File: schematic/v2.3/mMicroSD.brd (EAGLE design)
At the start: 38 x 18 mm, 23 parts, among them IC1 MAX3392, IC2 ATMEGA328, IC3 AD8531, J1 ISPTOUCH, M1 NTJD5121N

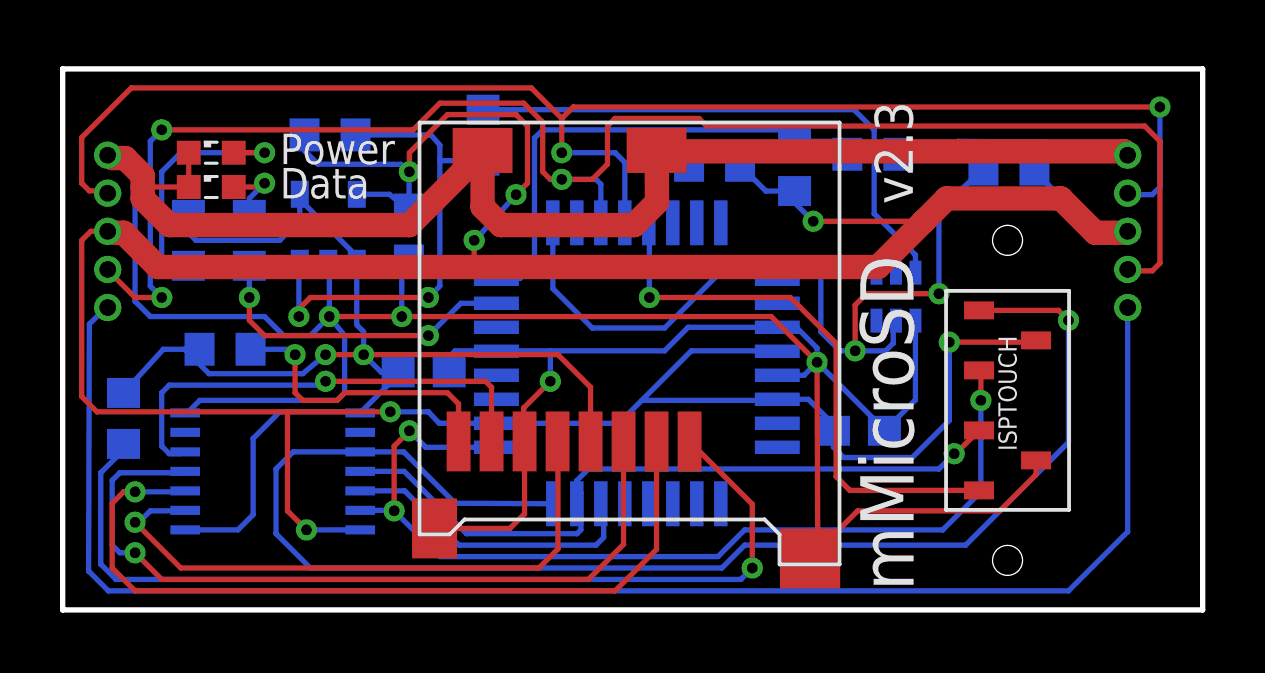
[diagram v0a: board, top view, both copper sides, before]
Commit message: Added some silkscreen to the board to make the orientation of two close resistors more apparent
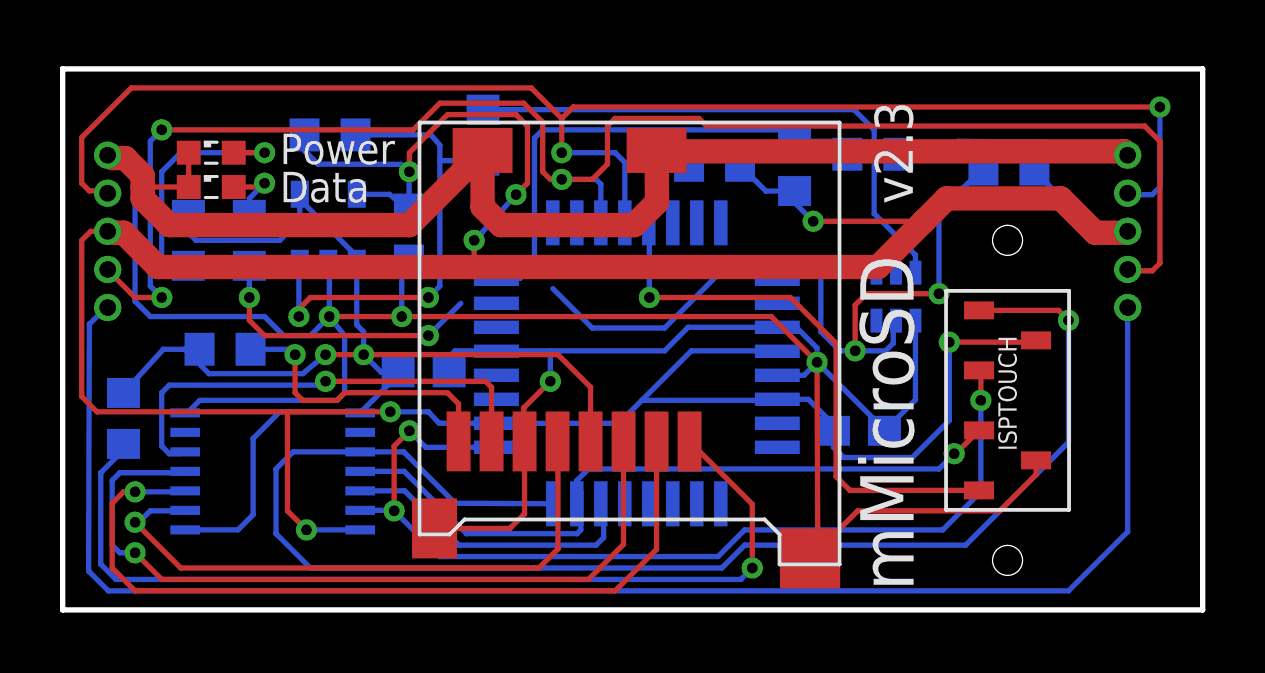
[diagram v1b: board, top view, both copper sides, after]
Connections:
- net N$10 renamed GATE
- net N$17 renamed ADC_LINE
- net N$3 renamed DATA_LED
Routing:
- net GATE: track 27.7 -> 25.5 mm
- net DATA_LED: track 10.7 -> 9.52 mm
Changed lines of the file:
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@@
 <?xml version="1.0" encoding="utf-8"?>
 <!DOCTYPE eagle SYSTEM "eagle.dtd">
-<eagle version="7.1.0">
+<eagle version="7.2.0">
 <drawing>
 <settings>
@@
 <text x="28.338990625" y="13.5300125" size="1.27" layer="21" font="vector" rot="R90">v2.3</text>
 <text x="7.239" y="14.859" size="1.016" layer="21" font="vector">Power</text>
-<text x="7.239" y="13.716" size="1.016" layer="21" font="vector">Data</text>
+<text x="7.239" y="13.589" size="1.016" layer="21" font="vector">Data</text>
+<wire x1="5.207" y1="11.176" x2="5.207" y2="13.335" width="0.4064" layer="22"/>
+<wire x1="6.985" y1="11.049" x2="6.985" y2="13.462" width="0.2032" layer="22"/>
+<wire x1="3.302" y1="13.462" x2="3.302" y2="11.049" width="0.2032" layer="22"/>
 </plain>
 <attributes>
@@
 <wire x1="4.203" y1="14.097" x2="2.667" y2="14.097" width="0.1778" layer="1"/>
 </signal>
-<signal name="N$10">
+<signal name="GATE">
 <contactref element="IC2" pad="25"/>
 <contactref element="M1" pad="2"/>
@@
 <wire x1="27.686" y1="8.89" x2="27.686" y2="9.552025" width="0.1778" layer="16"/>
 <wire x1="27.686" y1="9.552025" x2="27.7759125" y2="9.6419375" width="0.1778" layer="16"/>
-<wire x1="16.339925" y1="12.90348125" x2="16.339925" y2="10.711075" width="0.1778" layer="16"/>
 <wire x1="16.339925" y1="10.711075" x2="17.653" y2="9.398" width="0.1778" layer="16"/>
 <wire x1="17.653" y1="9.398" x2="20.066" y2="9.398" width="0.1778" layer="16"/>
@@
 <wire x1="29.21" y1="10.541" x2="29.21" y2="13.337909375" width="0.1778" layer="16"/>
 <wire x1="29.21" y1="13.337909375" x2="30.692103125" y2="14.6930125" width="0.1778" layer="16"/>
+<wire x1="16.339925" y1="10.711075" x2="16.339925" y2="12.90348125" width="0" layer="19" extent="16-16"/>
 </signal>
 <signal name="VCC_MBUS">
@@
 <wire x1="16.51" y1="5.603309375" x2="16.4970125" y2="5.616296875" width="0.1778" layer="1"/>
 </signal>
-<signal name="N$17">
+<signal name="ADC_LINE">
 <contactref element="R3" pad="1"/>
 <contactref element="R4" pad="2"/>
@@
 <wire x1="3.937" y1="15.24" x2="6.731" y2="15.24" width="0.1778" layer="16"/>
 </signal>
-<signal name="N$3">
+<signal name="DATA_LED">
 <contactref element="IC2" pad="23"/>
 <contactref element="R10" pad="2"/>
-<wire x1="14.457425" y1="10.22098125" x2="13.27401875" y2="10.22098125" width="0.1778" layer="16"/>
 <wire x1="13.27401875" y1="10.22098125" x2="12.192" y2="9.144" width="0.1778" layer="16"/>
 <via x="12.192" y="9.144" extent="1-16" drill="0.3556"/>
@@
 <wire x1="6.223" y1="10.414" x2="6.223" y2="11.469" width="0.1778" layer="16"/>
 <wire x1="6.731" y1="9.144" x2="12.192" y2="9.144" width="0.1778" layer="1"/>
+<wire x1="13.27401875" y1="10.22098125" x2="14.457425" y2="10.22098125" width="0" layer="19" extent="16-16"/>
 </signal>
 <signal name="N$4">
